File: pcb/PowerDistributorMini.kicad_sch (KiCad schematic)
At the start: 21 parts, among them J1 F1, J10 D2, J11 D3, J12 D4, J13 D5, J14 D6, J15 D7, J16 D8, J17 PWR, J2 F2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

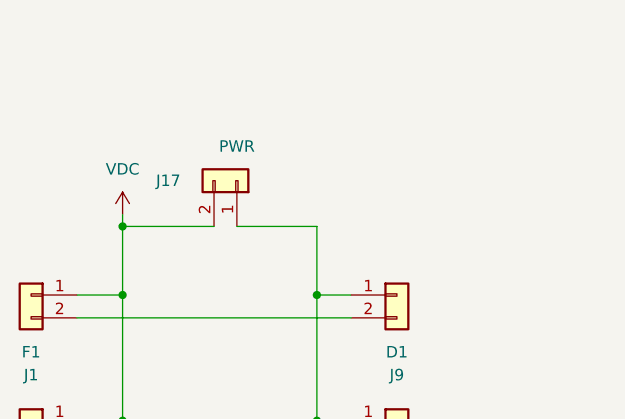
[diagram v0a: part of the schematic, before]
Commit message: v1.2 : alterative main connector; some markings
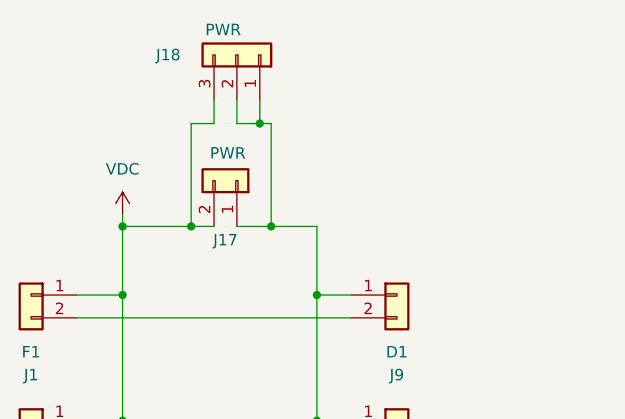
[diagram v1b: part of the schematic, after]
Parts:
- added J18: PWR, GSI_footprints:Wago-250-203, symbol Connector_Generic:Conn_01x03
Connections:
- net GND: now also J18.1 (Pin_1), J18.2 (Pin_2)
- net VDC: now also J18.3 (Pin_3)
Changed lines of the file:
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@@
 	(paper "A4")
 	(junction
+		(at 105.41 50.8)
+		(diameter 0)
+		(color 0 0 0 0)
+	)
+	(junction
 		(at 88.9 50.8)
 		(diameter 0)
@@
 	)
 	(junction
+		(at 104.14 39.37)
+		(diameter 0)
+		(color 0 0 0 0)
+	)
+	(junction
 		(at 110.49 72.39)
 		(diameter 0)
@@
 	)
 	(junction
+		(at 96.52 50.8)
+		(diameter 0)
+		(color 0 0 0 0)
+	)
+	(junction
 		(at 88.9 132.08)
 		(diameter 0)
@@
 	(wire
 		(pts
+			(xy 99.06 39.37) (xy 96.52 39.37)
+		)
+		(stroke
+			(width 0)
+			(type default)
+		)
+	)
+	(wire
+		(pts
+			(xy 99.06 36.83) (xy 99.06 39.37)
+		)
+		(stroke
+			(width 0)
+			(type default)
+		)
+	)
+	(wire
+		(pts
 			(xy 110.49 148.59) (xy 114.3 148.59)
 		)
@@
 	(wire
 		(pts
-			(xy 101.6 50.8) (xy 110.49 50.8)
+			(xy 101.6 50.8) (xy 105.41 50.8)
 		)
 		(stroke
@@
 	(wire
 		(pts
+			(xy 101.6 39.37) (xy 104.14 39.37)
+		)
+		(stroke
+			(width 0)
+			(type default)
+		)
+	)
+	(wire
+		(pts
+			(xy 104.14 39.37) (xy 105.41 39.37)
+		)
+		(stroke
+			(width 0)
+			(type default)
+		)
+	)
+	(wire
+		(pts
 			(xy 83.82 166.37) (xy 114.3 166.37)
 		)
@@
 	(wire
 		(pts
+			(xy 105.41 50.8) (xy 110.49 50.8)
+		)
+		(stroke
+			(width 0)
+			(type default)
+		)
+	)
+	(wire
+		(pts
+			(xy 104.14 36.83) (xy 104.14 39.37)
+		)
+		(stroke
+			(width 0)
+			(type default)
+		)
+	)
+	(wire
+		(pts
 			(xy 83.82 60.96) (xy 114.3 60.96)
 		)
@@
 	(wire
 		(pts
-			(xy 88.9 50.8) (xy 99.06 50.8)
+			(xy 88.9 50.8) (xy 96.52 50.8)
+		)
+		(stroke
+			(width 0)
+			(type default)
+		)
+	)
+	(wire
+		(pts
+			(xy 105.41 39.37) (xy 105.41 50.8)
 		)
 		(stroke
@@
 	(wire
 		(pts
+			(xy 96.52 50.8) (xy 99.06 50.8)
+		)
+		(stroke
+			(width 0)
+			(type default)
+		)
+	)
+	(wire
+		(pts
 			(xy 110.49 72.39) (xy 114.3 72.39)
 		)
@@
 	(wire
 		(pts
+			(xy 101.6 36.83) (xy 101.6 39.37)
+		)
+		(stroke
+			(width 0)
+			(type default)
+		)
+	)
+	(wire
+		(pts
 			(xy 83.82 102.87) (xy 114.3 102.87)
 		)
@@
 		(pts
 			(xy 88.9 132.08) (xy 88.9 148.59)
+		)
+		(stroke
+			(width 0)
+			(type default)
+		)
+	)
+	(wire
+		(pts
+			(xy 96.52 39.37) (xy 96.52 50.8)
 		)
 		(stroke
@@
 	)
 	(symbol
+		(lib_id "Connector_Generic:Conn_01x03")
+		(at 101.6 31.75 270)
+		(mirror x)
+		(unit 1)
+		(exclude_from_sim no)
+		(in_bom yes)
+		(on_board yes)
+		(dnp no)
+		(property "Reference" "J18"
+			(at 93.98 31.75 90)
+			(effects
+				(font
+					(size 1.27 1.27)
+				)
+			)
+		)
+		(property "Value" "PWR"
+			(at 100.076 28.956 90)
+			(effects
+				(font
+					(size 1.27 1.27)
+				)
+			)
+		)
+		(property "Footprint" "GSI_footprints:Wago-250-203"
+			(at 101.6 31.75 0)
+			(effects
+				(font
+					(size 1.27 1.27)
+				)
+				(hide yes)
+			)
+		)
+		(property "Datasheet" "~"
+			(at 101.6 31.75 0)
+			(effects
+				(font
+					(size 1.27 1.27)
+				)
+				(hide yes)
+			)
+		)
+		(property "Description" "Generic connector, single row, 01x03, script generated (kicad-library-utils/schlib/autogen/connector/)"
+			(at 101.6 31.75 0)
+			(effects
+				(font
+					(size 1.27 1.27)
+				)
+				(hide yes)
+			)
+		)
+		(pin "1"
+		)
+		(pin "2"
+		)
+		(pin "3"
+		)
+		(instances
+			(project "PowerDistributorMini"
+				(path "/f7e57650-fce6-4ad6-9815-aa132e016ba1"
+					(reference "J18")
+					(unit 1)
+				)
+			)
+		)
+	)
+	(symbol
 		(lib_id "Connector_Generic:Conn_01x02")
 		(at 101.6 45.72 270)
@@
 		(dnp no)
 		(property "Reference" "J17"
-			(at 93.98 45.72 90)
+			(at 100.33 52.324 90)
 			(effects
 				(font
@@
 		)
 		(property "Value" "PWR"
-			(at 101.6 41.91 90)
-			(effects
-				(font
+			(at 100.584 42.672 90)
+			(effects
+				(font
